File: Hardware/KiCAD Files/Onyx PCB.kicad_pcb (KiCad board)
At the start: 2 copper layers, 105.2 x 71.1 mm, 104 parts, among them J1 X Axis, J10 servo pins, J11 Conn_01x03_Male, J12 Screw_Terminal_01x02, J13 5V_Terminal, J14 3.3V_Terminal, J2 Y Axis, J3 Z Axis, J4 USB_B_Micro, J5 A Axis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

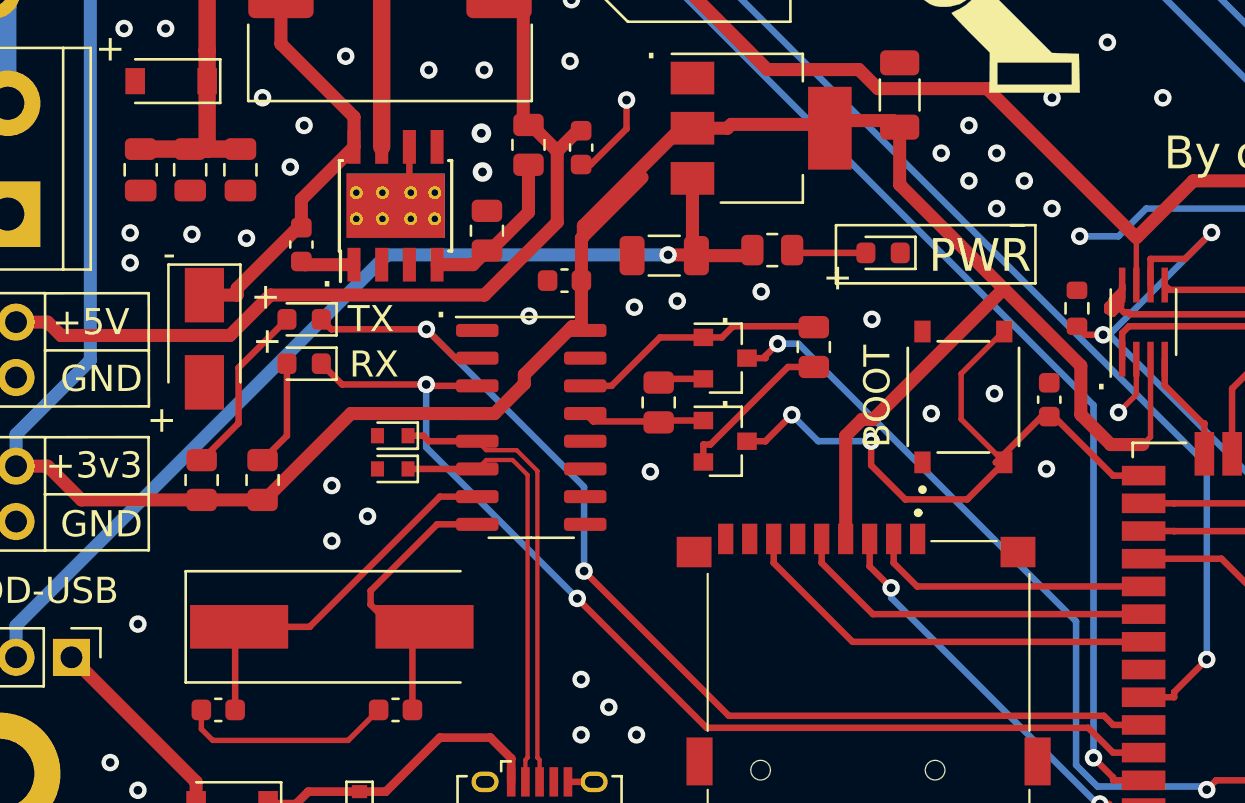
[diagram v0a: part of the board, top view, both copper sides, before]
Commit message: Added more GND Vias
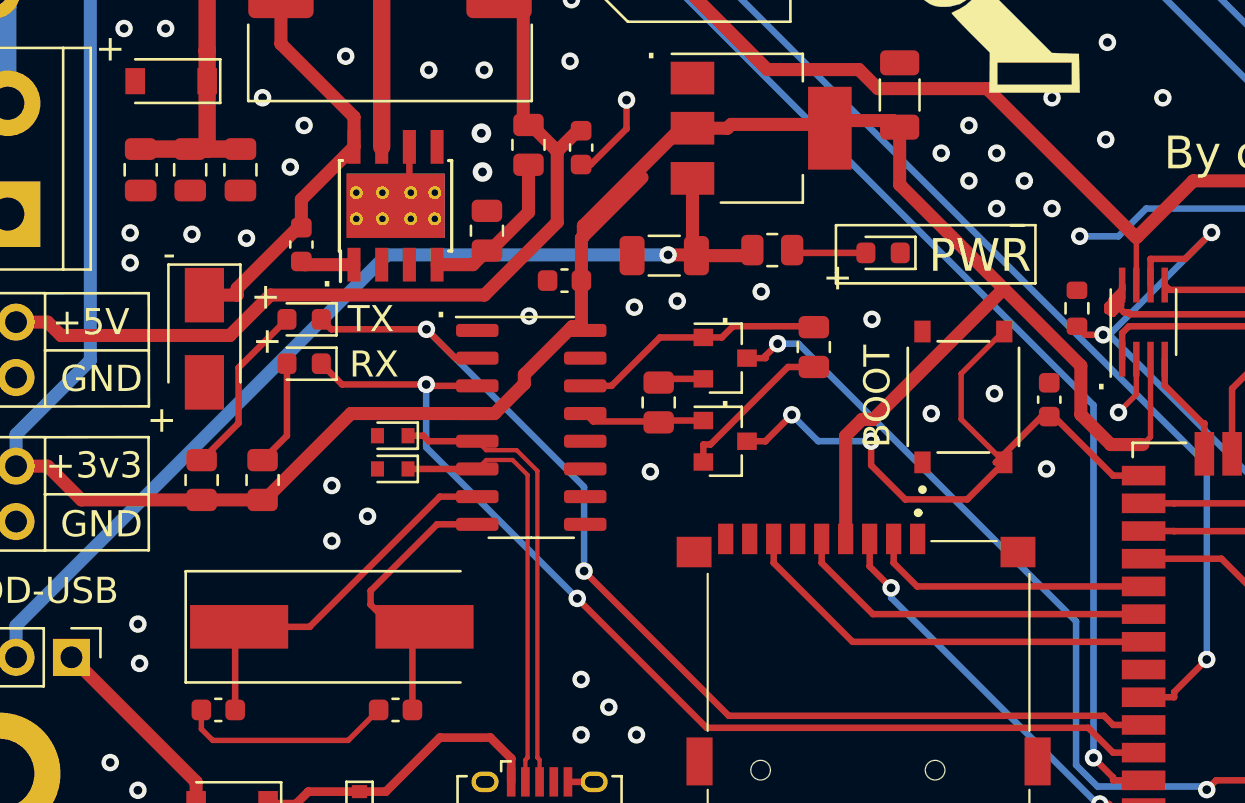
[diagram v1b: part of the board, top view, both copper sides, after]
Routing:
- net GND: vias 117 -> 119
